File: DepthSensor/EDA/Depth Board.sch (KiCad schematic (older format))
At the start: 19 parts, among them J1 Conn_01x04, J2 Conn_02x03_Odd_Even, J3 Screw_Terminal_01x03, U1 ATmega328P-AU, U2 74LVC1G126, U3 SN65HVD75, Y1 8MHz

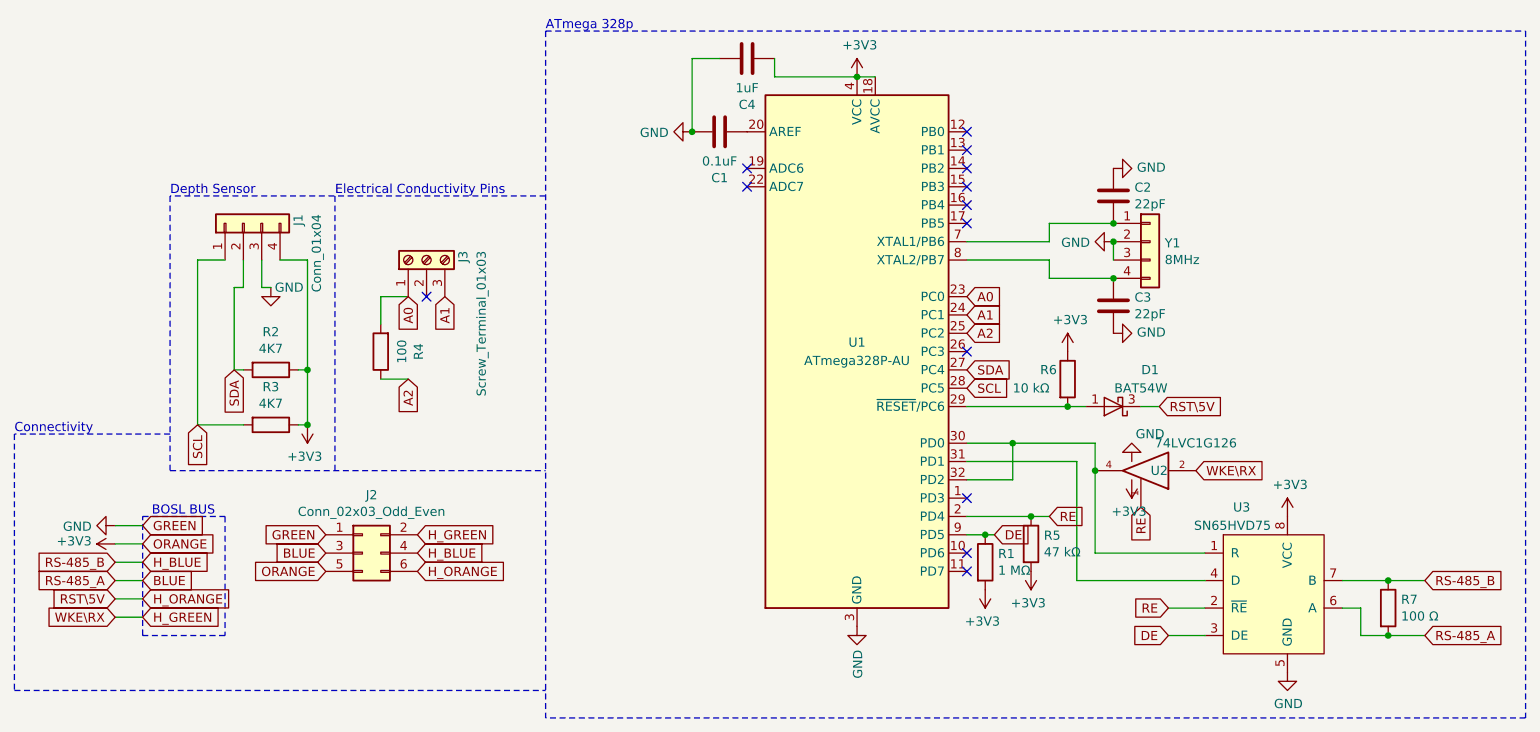
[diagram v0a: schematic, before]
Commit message: added documentation for depth sensor schematics
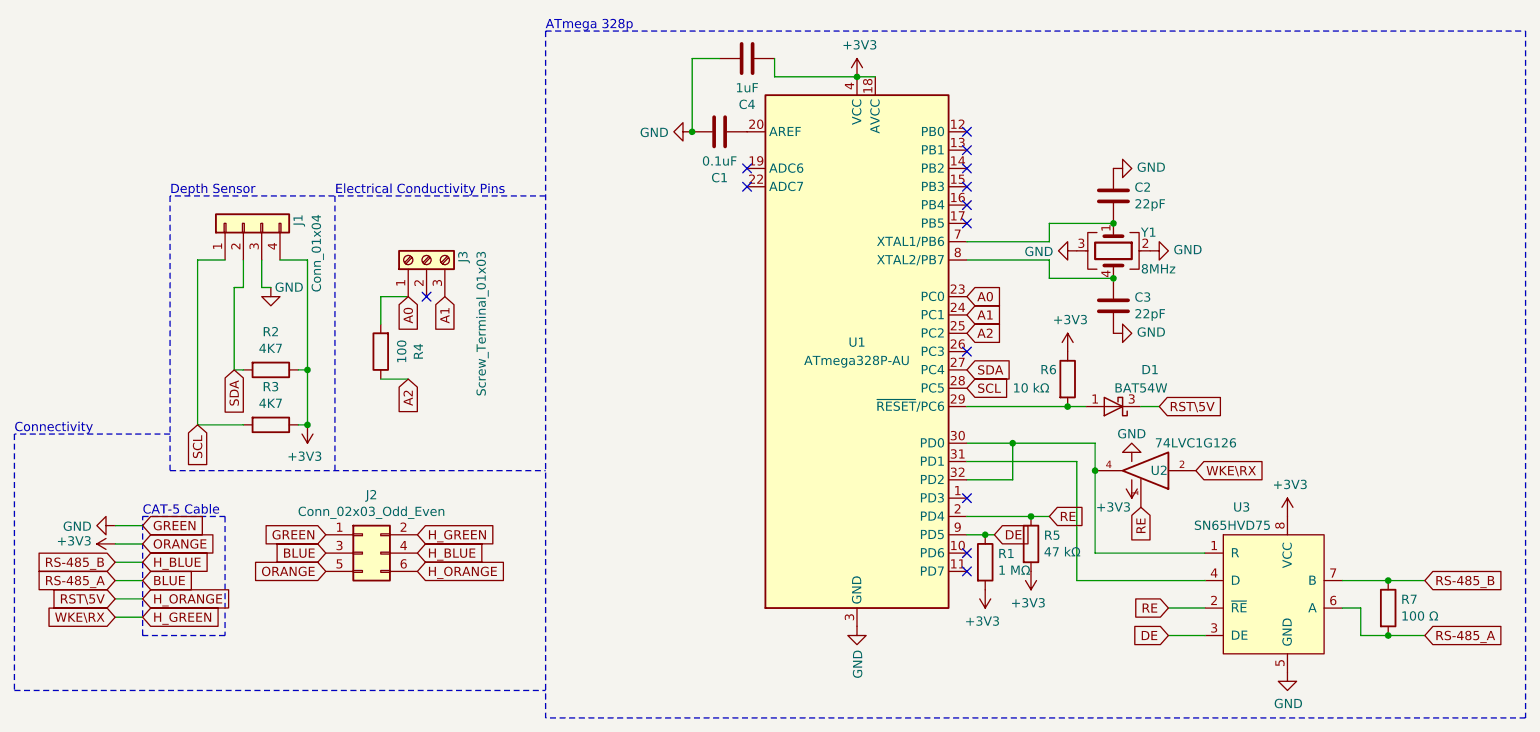
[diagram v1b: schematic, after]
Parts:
- removed Y1: 8MHz, SamacSys_Parts:Ralton_Crystal, symbol Connector_Generic:Conn_01x04
- added Y1: 8MHz, SamacSys_Parts:Ralton_Crystal, symbol Device:Crystal_GND23
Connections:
- net GND: now also Y1.2, Y1.3
- net at C2.2, U1.7 (XTAL1/PB6): now also Y1.1
- net at C3.1, U1.8 (XTAL2/PB7): now also Y1.4
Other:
- note added: "CAT-5 Cable"
- note removed: "BOSL BUS"
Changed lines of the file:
@@
 encoding utf-8
 Sheet 1 1
-Title ""
-Date ""
-Rev ""
-Comp ""
+Title "RS-485 All-in-one Probe"
+Date "2020-11-18"
+Rev "0.1.0"
+Comp "Monash BoSL"
 Comment1 ""
 Comment2 ""
@@
 Wire Wire Line
 	2200 3850 2200 4750
-$Comp
-L MCU_Microchip_ATmega:ATmega328P-AU U1
-U 1 1 5F06A751
-P 5800 4350
-F 0 "U1" H 5800 4400 50  0000 C CNN
-F 1 "ATmega328P-AU" H 5800 4300 50  0000 C CNN
-F 2 "Package_QFP:TQFP-32_7x7mm_P0.8mm" H 5800 4350 50  0001 C CIN
-F 3 "http://ww1.microchip.com/downloads/en/DeviceDoc/ATmega328_P%20AVR%20MCU%20with%20picoPower%20Technology%20Data%20Sheet%2040001984A.pdf" H 5800 4350 50  0001 C CNN
-	1    5800 4350
-	1    0    0    -1
-$EndComp
 $Comp
 L power:+3V3 #PWR0101
@@
 	4900 2750 4900 3150
 Connection ~ 4900 3150
-$Comp
-L Connector_Generic:Conn_01x04 Y1
-U 1 1 5F0833E4
-P 7400 3750
-F 0 "Y1" H 7480 3742 50  0000 L CNN
-F 1 "8MHz" H 7480 3651 50  0000 L CNN
-F 2 "SamacSys_Parts:Ralton_Crystal" H 7400 3750 50  0001 C CNN
-F 3 "~" H 7400 3750 50  0001 C CNN
-	1    7400 3750
-	1    0    0    -1
-$EndComp
-$Comp
-L power:GND #PWR0103
-U 1 1 5F0841E6
-P 7200 3750
-F 0 "#PWR0103" H 7200 3500 50  0001 C CNN
-F 1 "GND" V 7205 3622 50  0000 R CNN
-F 2 "" H 7200 3750 50  0001 C CNN
-F 3 "" H 7200 3750 50  0001 C CNN
-	1    7200 3750
-	0    1    1    0
-$EndComp
-Wire Wire Line
-	7200 3850 7200 3750
-Connection ~ 7200 3750
 Wire Wire Line
 	6400 3850 6850 3850
@@
 Wire Wire Line
 	6850 3950 7200 3950
-Connection ~ 7200 3950
 Wire Wire Line
 	6400 3750 6850 3750
@@
 Wire Wire Line
 	6850 3650 7200 3650
-Connection ~ 7200 3650
 Text GLabel 1900 5800 2    50   Input ~ 0
 H_GREEN
@@
 Wire Notes Line
 	1900 5900 1900 5250
-Text Notes 1950 5250 0    50   ~ 0
-BOSL BUS
+Text Notes 1900 5250 0    50   ~ 0
+CAT-5 Cable
 Wire Wire Line
 	1900 5800 1750 5800
@@
 P 7300 5050
 F 0 "#PWR06" H 7300 4900 50  0001 C CNN
-F 1 "+3V3" H 7315 5223 50  0000 C CNN
+F 1 "+3V3" H 7400 5200 50  0000 C CNN
 F 2 "" H 7300 5050 50  0001 C CNN
 F 3 "" H 7300 5050 50  0001 C CNN
@@
 P 7300 4950
 F 0 "#PWR07" H 7300 4700 50  0001 C CNN
-F 1 "GND" H 7200 4800 50  0000 C CNN
+F 1 "GND" H 7300 4800 50  0000 C CNN
 F 2 "" H 7300 4950 50  0001 C CNN
 F 3 "" H 7300 4950 50  0001 C CNN
@@
 	-1   0    0    1
 $EndComp
+$Comp
+L Device:Crystal_GND23 Y1
+U 1 1 5FB48044
+P 7200 3800
+F 0 "Y1" V 7100 3950 50  0000 L CNN
+F 1 "8MHz" V 7300 3950 50  0000 L CNN
+F 2 "SamacSys_Parts:Ralton_Crystal" H 7200 3800 50  0001 C CNN
+F 3 "~" H 7200 3800 50  0001 C CNN
+	1    7200 3800
+	0    1    1    0
+$EndComp
+Connection ~ 7200 3650
+Connection ~ 7200 3950
+$Comp
+L power:GND #PWR?
+U 1 1 5FB4956B
+P 7000 3800
+F 0 "#PWR?" H 7000 3550 50  0001 C CNN
+F 1 "GND" V 7005 3672 50  0000 R CNN
+F 2 "" H 7000 3800 50  0001 C CNN
+F 3 "" H 7000 3800 50  0001 C CNN
+	1    7000 3800
+	0    1    1    0
+$EndComp
+$Comp
+L power:GND #PWR?
+U 1 1 5FB49C76
+P 7400 3800
+F 0 "#PWR?" H 7400 3550 50  0001 C CNN
+F 1 "GND" V 7405 3672 50  0000 R CNN
+F 2 "" H 7400 3800 50  0001 C CNN
+F 3 "" H 7400 3800 50  0001 C CNN
+	1    7400 3800
+	0    -1   -1   0
+$EndComp
+$Comp
+L MCU_Microchip_ATmega:ATmega328P-AU U1
+U 1 1 5F06A751
+P 5800 4350
+F 0 "U1" H 5800 4400 50  0000 C CNN
+F 1 "ATmega328P-AU" H 5800 4300 50  0000 C CNN
+F 2 "Package_QFP:TQFP-32_7x7mm_P0.8mm" H 5800 4350 50  0001 C CIN
+F 3 "http://ww1.microchip.com/downloads/en/DeviceDoc/ATmega328_P%20AVR%20MCU%20with%20picoPower%20Technology%20Data%20Sheet%2040001984A.pdf" H 5800 4350 50  0001 C CNN
+	1    5800 4350
+	1    0    0    -1
+$EndComp
 $EndSCHEMATC
